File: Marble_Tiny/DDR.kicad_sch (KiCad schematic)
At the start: 53 parts, among them U2 AS4C256M16D3

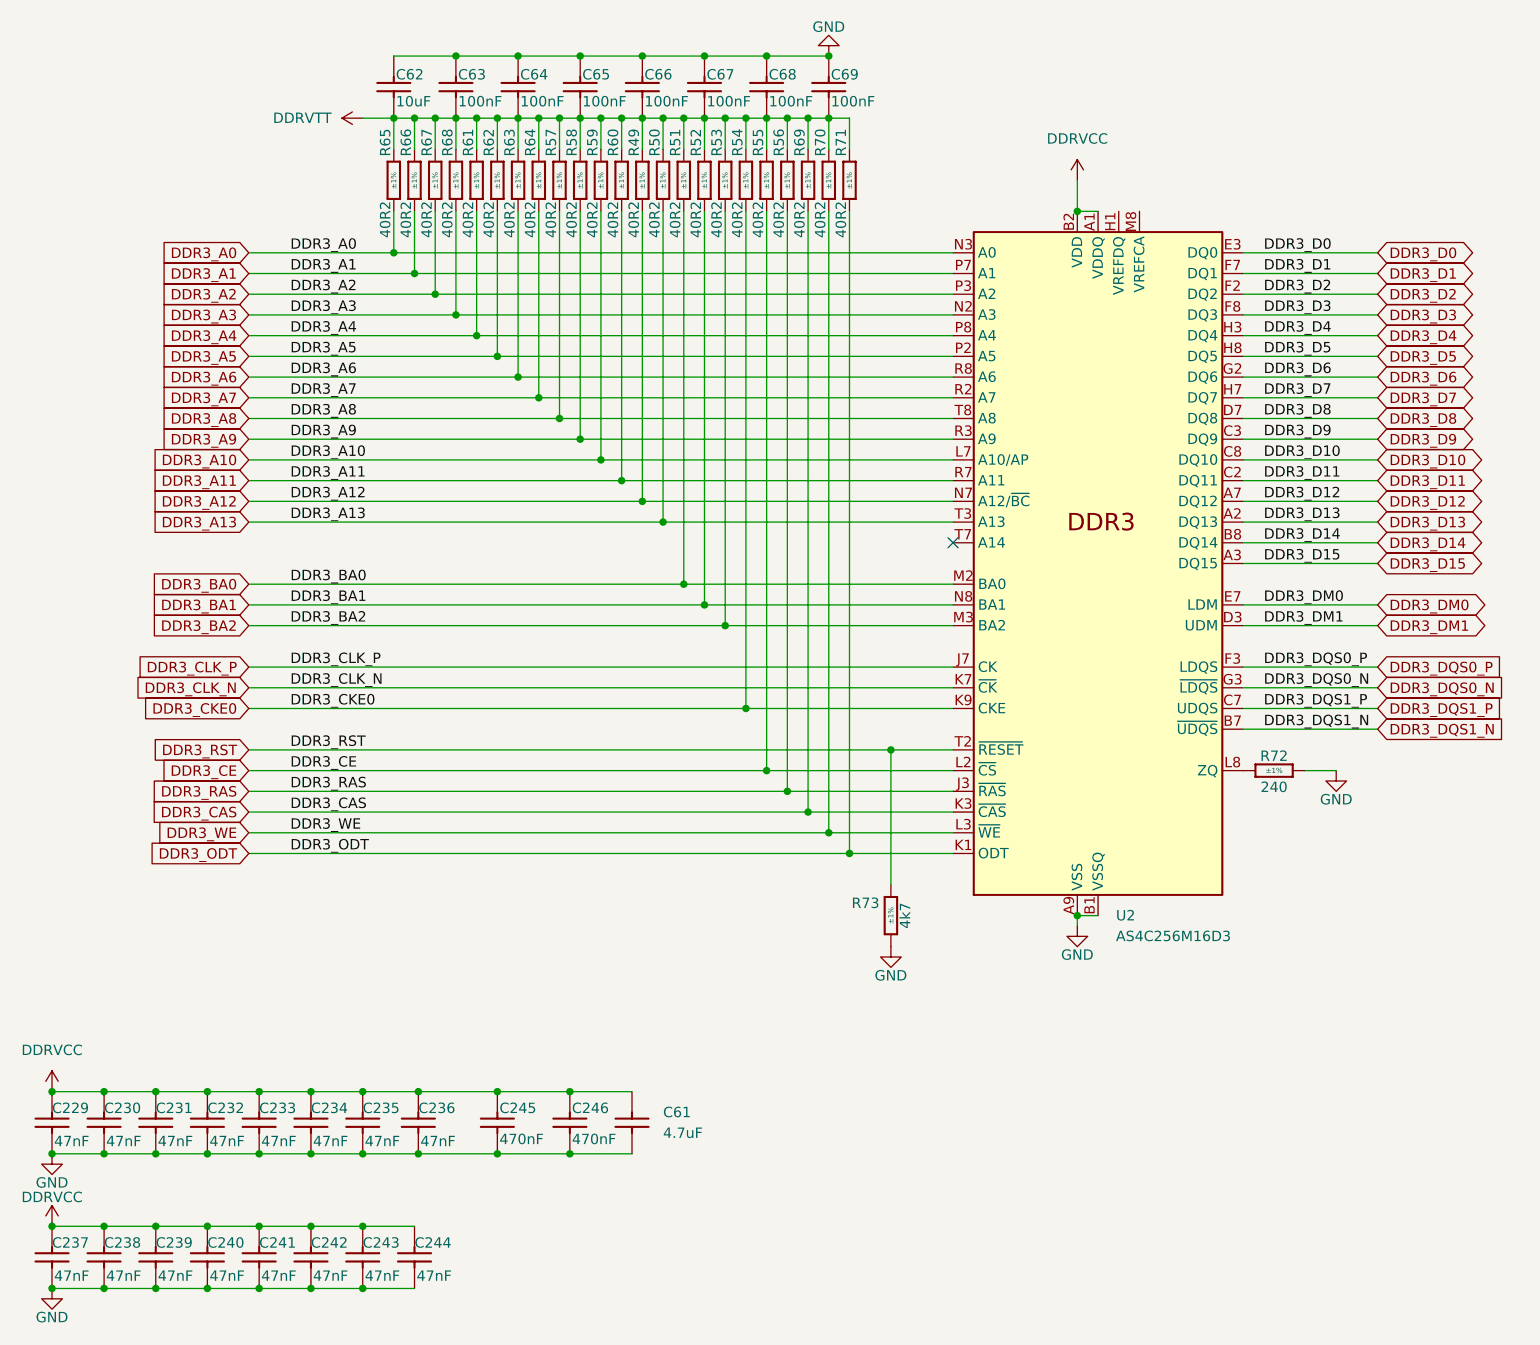
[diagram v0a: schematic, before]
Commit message: fixed ERCs; added test points; added WP switch
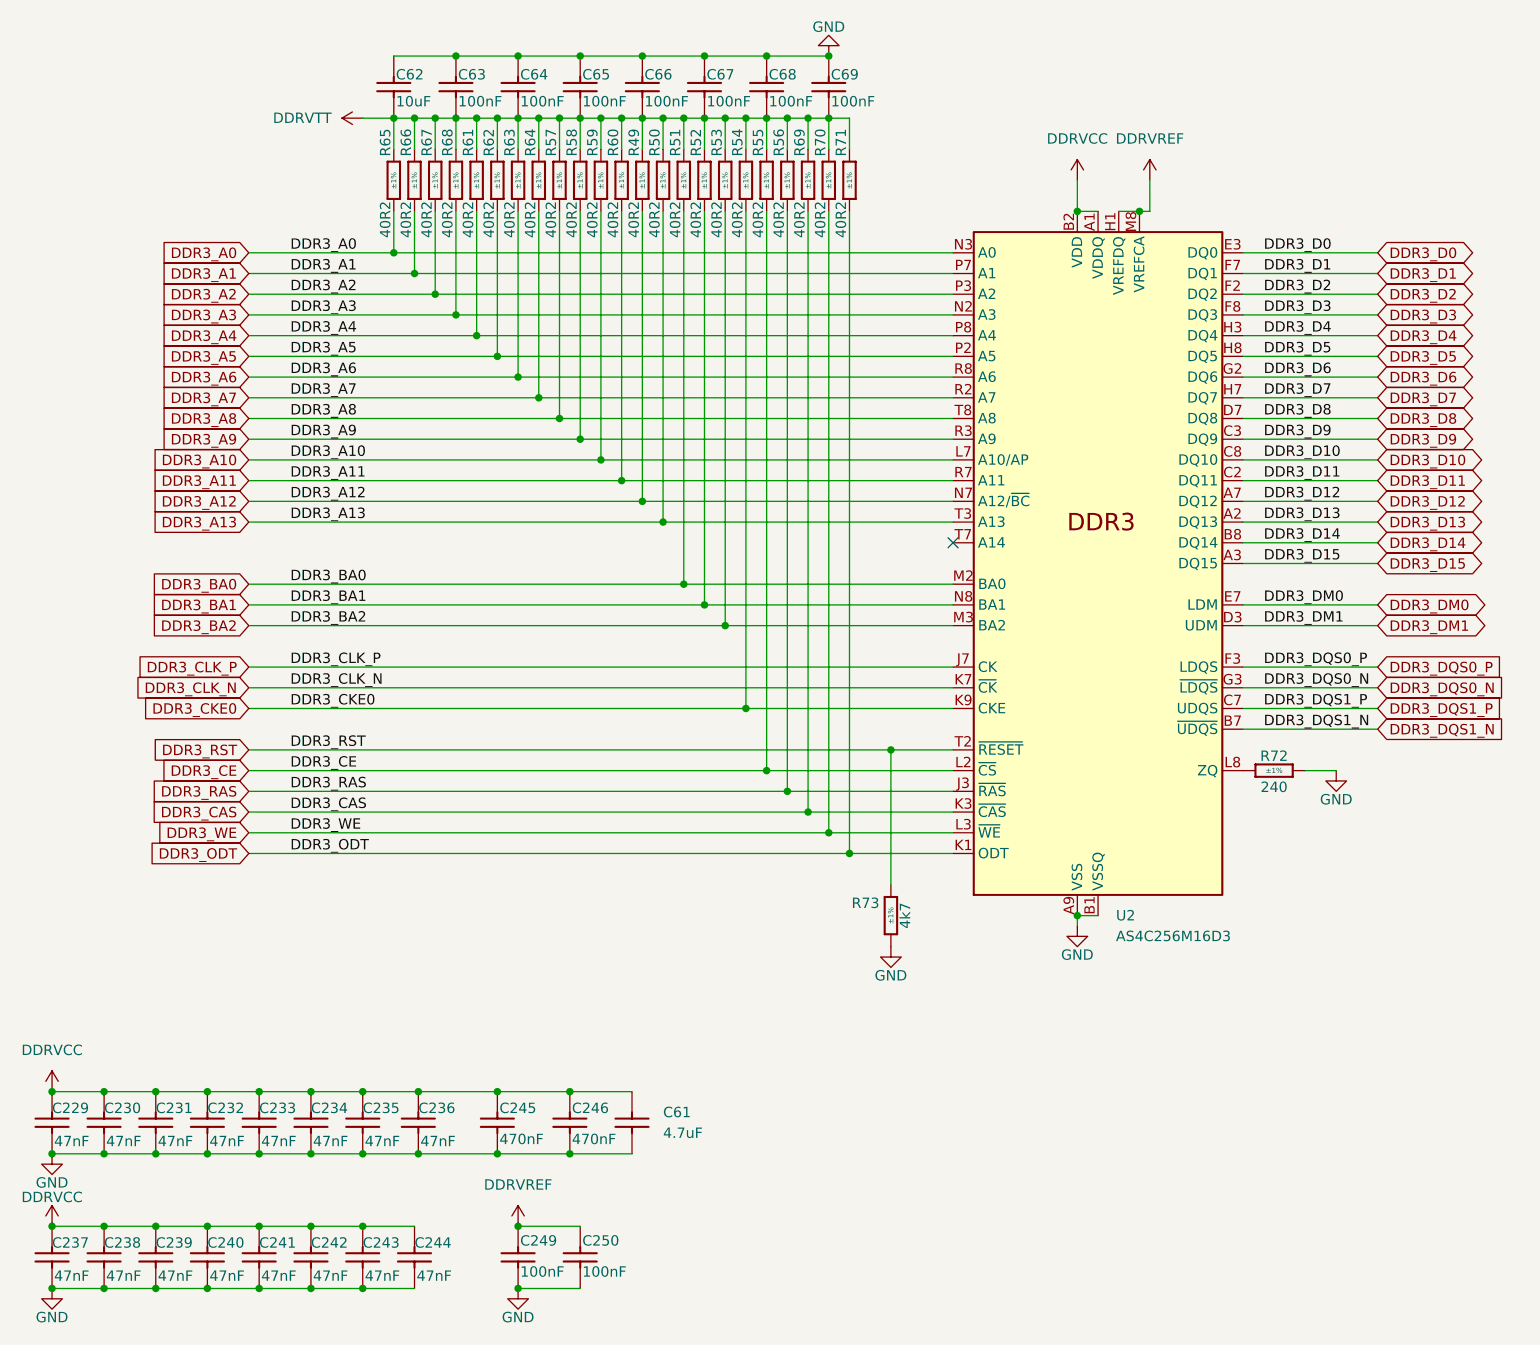
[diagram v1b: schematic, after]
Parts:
- added C249, C250: CC0201_100NF_6.3V_10%_X5R, Capacitors SMD:CAPC0603X33N, symbol Capacitors SMD:CC0201_100NF_6.3V_10%_X5R
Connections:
- net GND: now also C249.1, C250.1
- net DDRVREF: now reaches U2.H1 (VREFDQ)
- net DDRVREF: now also U2.M8 (VREFCA), C249.2, C250.2

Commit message: fixed issue with PMODs; added board name and revision; fixed polygons issue
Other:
- company: (none) -> ${name}
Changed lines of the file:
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@@
 	(generator_version "9.0")
 	(paper "A4")
+	(title_block
+		(date "2025-04-18")
+		(rev "${rev}")
+		(company "${name}")
+		(comment 1 "${author}")
+	)
 	(junction
 		(at 91.44 40.64)
